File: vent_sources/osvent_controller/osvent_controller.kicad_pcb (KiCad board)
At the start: 2 copper layers, 151.1 x 76.8 mm, 56 parts, among them J1 SOLENOID_A, J2 SWITCH_A, J3 SWITCH_B, J4 SOLENOID_B, J5 POWER, J6 STEPPER, J7 PRESSURE_SENSOR, J8 TFT_DISPLAY, J9 SPEAKER, K1 G5V-2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

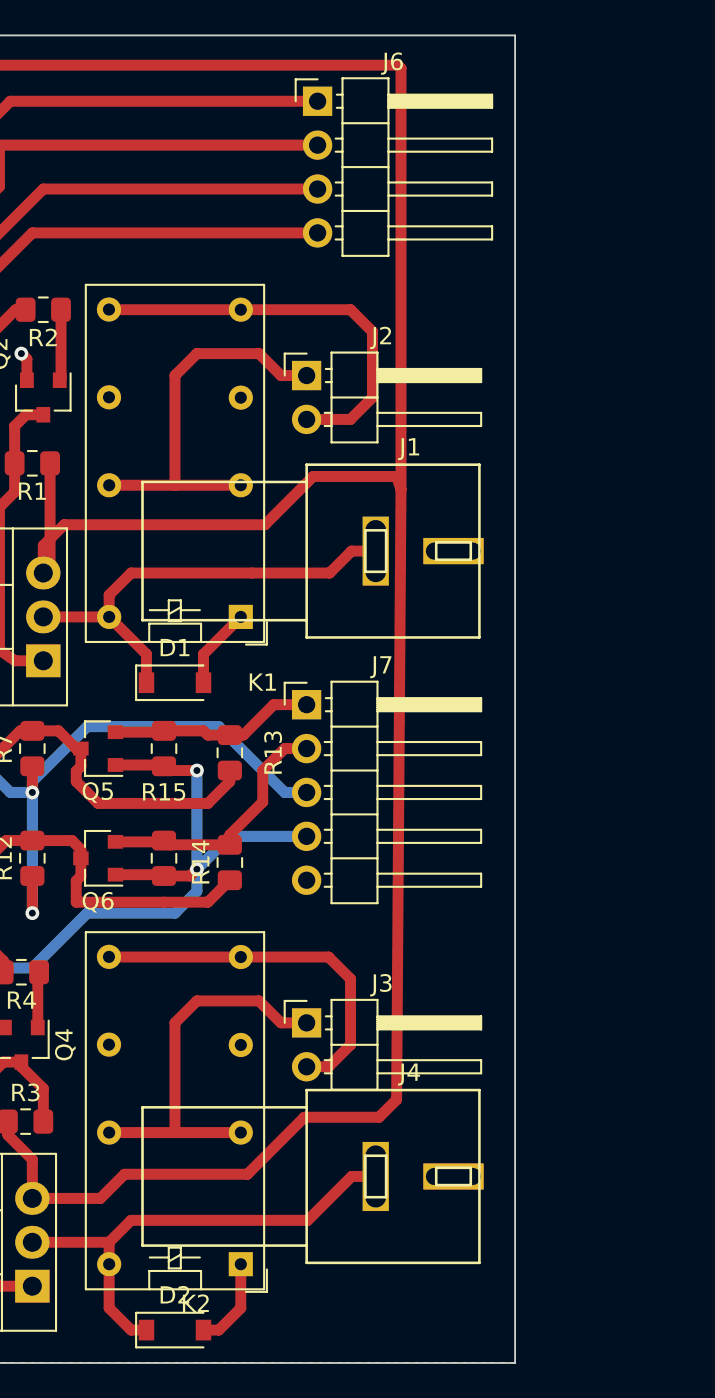
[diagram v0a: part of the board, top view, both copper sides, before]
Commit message: Flipped the RCA connectors around
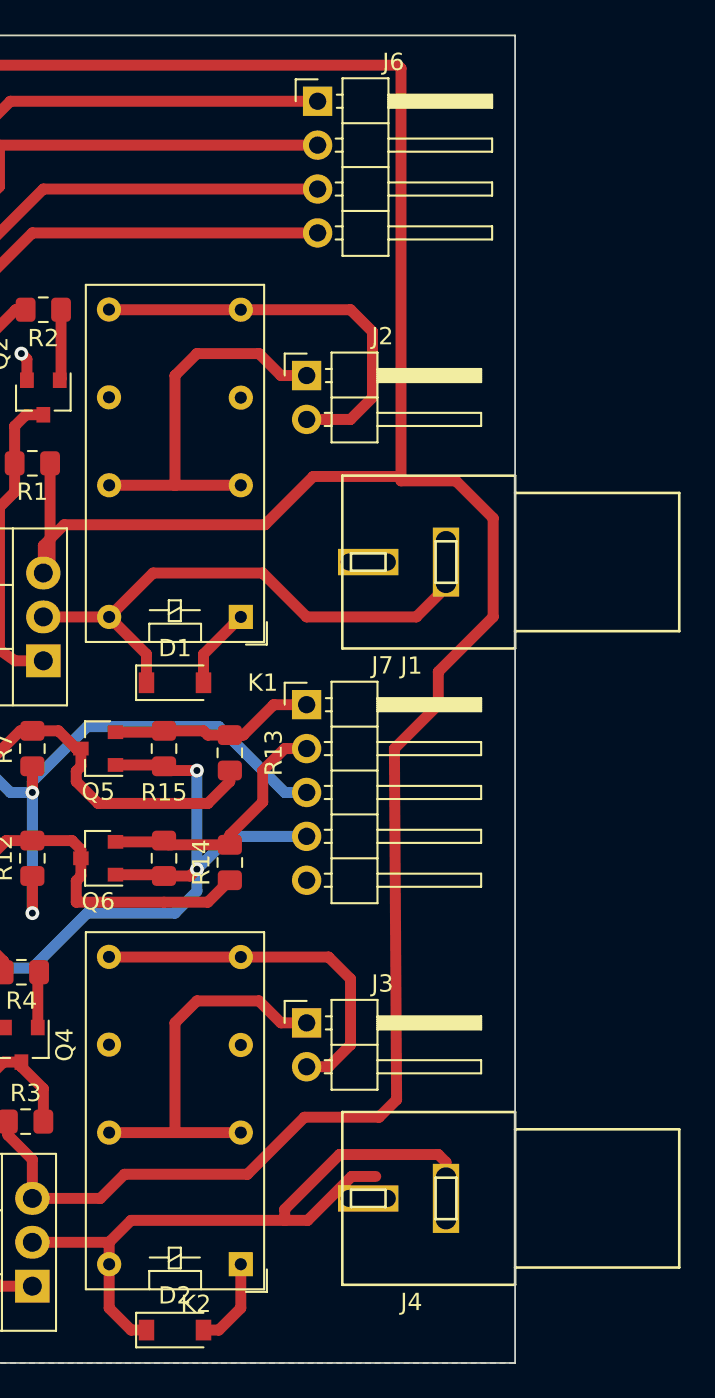
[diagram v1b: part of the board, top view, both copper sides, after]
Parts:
- moved J4 12.1 mm to (171.4, 89.5), turned to 180 degrees
- moved J1 12.1 mm to (171.4, 52.7), turned to 180 degrees
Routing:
- net Net-(D2-Pad1): track 27.9 -> 41.5 mm
- net Net-(D1-Pad1): track 26.3 -> 32.3 mm
- net +12V: track 247.0 -> 252.6 mm
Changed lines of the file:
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@@
     (thickness 1.6)
     (drawings 4)
-    (tracks 570)
+    (tracks 581)
     (zones 0)
     (modules 56)
@@
   )
   (module library:Kycon_KLPX-0848A-2-x (layer F.Cu)
-    (at 159.385 52.07)
+    (at 171.45 52.705 180)
     (fp_text reference J1 (at 6 -6 180) (layer F.SilkS)
       (effects (font (size 1 1) (thickness 0.15)))
@@
     (fp_line (start 0 -5) (end 10 -5) (layer F.SilkS) (width 0.15))
     (fp_line (start 0 -4) (end 0 -5) (layer F.SilkS) (width 0.15))
-    (pad 1 thru_hole rect (at 8.5 0) (size 3.5 1.524) (drill oval 3.2 1) (layers *.Cu *.Mask)
+    (pad 1 thru_hole rect (at 8.5 0 180) (size 3.5 1.524) (drill oval 3.2 1) (layers *.Cu *.Mask)
       (net 5 GNDREF))
-    (pad 2 thru_hole rect (at 4 0) (size 1.524 4) (drill oval 1.2 3.6) (layers *.Cu *.Mask)
+    (pad 2 thru_hole rect (at 4 0 180) (size 1.524 4) (drill oval 1.2 3.6) (layers *.Cu *.Mask)
       (net 45 "Net-(D1-Pad1)"))
   )
@@
   )
   (module library:Kycon_KLPX-0848A-2-x (layer F.Cu)
-    (at 159.385 88.265)
+    (at 171.45 89.535 180)
     (fp_text reference J4 (at 6 -6 180) (layer F.SilkS)
       (effects (font (size 1 1) (thickness 0.15)))
@@
     (fp_line (start 0 -5) (end 10 -5) (layer F.SilkS) (width 0.15))
     (fp_line (start 0 -4) (end 0 -5) (layer F.SilkS) (width 0.15))
-    (pad 1 thru_hole rect (at 8.5 0) (size 3.5 1.524) (drill oval 3.2 1) (layers *.Cu *.Mask)
+    (pad 1 thru_hole rect (at 8.5 0 180) (size 3.5 1.524) (drill oval 3.2 1) (layers *.Cu *.Mask)
       (net 5 GNDREF))
-    (pad 2 thru_hole rect (at 4 0) (size 1.524 4) (drill oval 1.2 3.6) (layers *.Cu *.Mask)
+    (pad 2 thru_hole rect (at 4 0 180) (size 1.524 4) (drill oval 1.2 3.6) (layers *.Cu *.Mask)
       (net 46 "Net-(D2-Pad1)"))
   )
@@
   (segment (start 142.095 85.09) (end 142.095 85.87) (width 0.635) (layer F.Cu) (net 30))
   (segment (start 142.095 85.87) (end 143.51 87.285) (width 0.635) (layer F.Cu) (net 30))
-  (segment (start 144.145 51.7525) (end 144.145 53.34) (width 0.635) (layer F.Cu) (net 30))
-  (segment (start 145.3515 50.546) (end 144.145 51.7525) (width 0.635) (layer F.Cu) (net 30))
-  (segment (start 156.972 50.546) (end 145.3515 50.546) (width 0.635) (layer F.Cu) (net 30))
-  (segment (start 159.766 47.752) (end 156.972 50.546) (width 0.635) (layer F.Cu) (net 30))
-  (segment (start 164.592 47.752) (end 159.766 47.752) (width 0.635) (layer F.Cu) (net 30))
   (segment (start 143.51 89.535) (end 147.447 89.535) (width 0.635) (layer F.Cu) (net 30))
   (segment (start 155.956 88.138) (end 159.258 84.836) (width 0.635) (layer F.Cu) (net 30))
@@
   (segment (start 139.88099 23.94901) (end 164.66501 23.94901) (width 0.635) (layer F.Cu) (net 30))
   (segment (start 137.16 26.67) (end 139.88099 23.94901) (width 0.635) (layer F.Cu) (net 30))
-  (segment (start 164.846 24.13) (end 164.846 48.514) (width 0.635) (layer F.Cu) (net 30))
-  (segment (start 164.592 83.82) (end 164.846 48.514) (width 0.635) (layer F.Cu) (net 30))
   (segment (start 164.66501 23.94901) (end 164.846 24.13) (width 0.635) (layer F.Cu) (net 30))
-  (segment (start 164.846 48.514) (end 164.592 47.752) (width 0.635) (layer F.Cu) (net 30))
   (segment (start 63.5 26.035) (end 63.5 33.02) (width 0.635) (layer F.Cu) (net 30))
   (segment (start 65.659 23.876) (end 63.5 26.035) (width 0.635) (layer F.Cu) (net 30))
   (segment (start 137.16 26.67) (end 134.366 23.876) (width 0.635) (layer F.Cu) (net 30))
   (segment (start 134.366 23.876) (end 65.659 23.876) (width 0.635) (layer F.Cu) (net 30))
+  (segment (start 164.846 48.006) (end 168.021 48.006) (width 0.635) (layer F.Cu) (net 30))
+  (segment (start 164.846 24.13) (end 164.846 48.006) (width 0.635) (layer F.Cu) (net 30))
+  (segment (start 168.021 48.006) (end 170.18 50.165) (width 0.635) (layer F.Cu) (net 30))
+  (segment (start 170.18 50.165) (end 170.18 55.88) (width 0.635) (layer F.Cu) (net 30))
+  (segment (start 170.18 55.88) (end 167.005 59.055) (width 0.635) (layer F.Cu) (net 30))
+  (segment (start 167.005 59.055) (end 167.005 60.96) (width 0.635) (layer F.Cu) (net 30))
+  (segment (start 167.005 60.96) (end 164.465 63.5) (width 0.635) (layer F.Cu) (net 30))
+  (segment (start 164.592 83.82) (end 164.465 63.5) (width 0.635) (layer F.Cu) (net 30))
+  (segment (start 164.592 47.752) (end 159.766 47.752) (width 0.635) (layer F.Cu) (net 30))
+  (segment (start 159.766 47.752) (end 156.972 50.546) (width 0.635) (layer F.Cu) (net 30))
+  (segment (start 156.972 50.546) (end 145.3515 50.546) (width 0.635) (layer F.Cu) (net 30))
+  (segment (start 145.3515 50.546) (end 144.145 51.7525) (width 0.635) (layer F.Cu) (net 30))
+  (segment (start 144.145 51.7525) (end 144.145 53.34) (width 0.635) (layer F.Cu) (net 30))
   (segment (start 160.02 26.035) (end 142.24 26.035) (width 0.635) (layer F.Cu) (net 31))
   (segment (start 142.24 26.035) (end 140.335 27.94) (width 0.635) (layer F.Cu) (net 31))
@@
   (segment (start 88.225 29.25) (end 97.79 29.25) (width 0.635) (layer F.Cu) (net 44))
   (segment (start 85.725 31.75) (end 88.225 29.25) (width 0.635) (layer F.Cu) (net 44))
-  (segment (start 149.225 53.34) (end 147.955 54.61) (width 0.635) (layer F.Cu) (net 45))
   (segment (start 150.115 59.69) (end 150.115 58.04) (width 0.635) (layer F.Cu) (net 45))
-  (segment (start 147.955 54.61) (end 147.955 55.88) (width 0.635) (layer F.Cu) (net 45))
   (segment (start 150.115 58.04) (end 147.955 55.88) (width 0.635) (layer F.Cu) (net 45))
   (segment (start 147.955 55.88) (end 144.145 55.88) (width 0.635) (layer F.Cu) (net 45))
-  (segment (start 161.988 52.07) (end 160.718 53.34) (width 0.635) (layer F.Cu) (net 45))
-  (segment (start 160.718 53.34) (end 156.21 53.34) (width 0.635) (layer F.Cu) (net 45))
-  (segment (start 163.385 52.07) (end 161.988 52.07) (width 0.635) (layer F.Cu) (net 45))
-  (segment (start 156.21 53.34) (end 149.225 53.34) (width 0.635) (layer F.Cu) (net 45))
+  (segment (start 167.45 52.705) (end 167.45 54.165) (width 0.635) (layer F.Cu) (net 45))
+  (segment (start 167.45 54.165) (end 165.735 55.88) (width 0.635) (layer F.Cu) (net 45))
+  (segment (start 165.735 55.88) (end 159.385 55.88) (width 0.635) (layer F.Cu) (net 45))
+  (segment (start 159.385 55.88) (end 156.845 53.34) (width 0.635) (layer F.Cu) (net 45))
+  (segment (start 156.845 53.34) (end 150.495 53.34) (width 0.635) (layer F.Cu) (net 45))
+  (segment (start 150.495 53.34) (end 147.955 55.88) (width 0.635) (layer F.Cu) (net 45))
   (segment (start 147.955 95.885) (end 149.225 97.155) (width 0.635) (layer F.Cu) (net 46))
   (segment (start 147.955 92.075) (end 147.955 93.345) (width 0.635) (layer F.Cu) (net 46))
@@
   (segment (start 147.955 93.345) (end 147.955 95.885) (width 0.635) (layer F.Cu) (net 46))
   (segment (start 149.225 90.805) (end 147.955 92.075) (width 0.635) (layer F.Cu) (net 46))
-  (segment (start 159.448 90.805) (end 149.225 90.805) (width 0.635) (layer F.Cu) (net 46))
   (segment (start 161.988 88.265) (end 159.448 90.805) (width 0.635) (layer F.Cu) (net 46))
   (segment (start 163.385 88.265) (end 161.988 88.265) (width 0.635) (layer F.Cu) (net 46))
+  (segment (start 158.115 90.805) (end 149.225 90.805) (width 0.635) (layer F.Cu) (net 46))
+  (segment (start 159.448 90.805) (end 158.115 90.805) (width 0.635) (layer F.Cu) (net 46))
+  (segment (start 167.45 87.44) (end 167.45 89.535) (width 0.635) (layer F.Cu) (net 46))
+  (segment (start 167.005 86.995) (end 167.45 87.44) (width 0.635) (layer F.Cu) (net 46))
+  (segment (start 161.29 86.995) (end 167.005 86.995) (width 0.635) (layer F.Cu) (net 46))
+  (segment (start 158.115 90.805) (end 158.115 90.17) (width 0.635) (layer F.Cu) (net 46))
+  (segment (start 158.115 90.17) (end 161.29 86.995) (width 0.635) (layer F.Cu) (net 46))
   (segment (start 159.385 44.45) (end 161.925 44.45) (width 0.635) (layer F.Cu) (net 47))
   (segment (start 161.925 38.1) (end 155.575 38.1) (width 0.635) (layer F.Cu) (net 47))
@@
     (connect_pads (clearance 0.508))
     (min_thickness 0.254)
-    (fill yes (arc_segments 32) (thermal_gap 0.508) (thermal_bridge_width 0.508))
+    (fill (arc_segments 32) (thermal_gap 0.508) (thermal_bridge_width 0.508))
     (polygon
       (pts

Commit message: Removed relays, added extra connector, surge cap
1. Removed the PCB mounted relays. Instead use outboard relays of appropriate rating.
2. Added a 47uf close to A4988 to protect from ESD/surge
3. Added a new connector with A6,A7, D7, +5 and ground for analog sensors
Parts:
- removed J2: SWITCH_A, Connector_PinHeader_2.54mm:PinHeader_1x02_P2.54mm_Horizontal
- removed J3: SWITCH_B, Connector_PinHeader_2.54mm:PinHeader_1x02_P2.54mm_Horizontal
- removed K1, K2: G5V-2, Relay_THT:Relay_DPDT_Omron_G5V-2
- added C10: 47u, Capacitor_THT:CP_Radial_D5.0mm_P2.50mm, F.Cu at (143.5, 28.6)
- added J10: EXTENSION PORT, Connector_PinHeader_2.54mm:PinHeader_1x05_P2.54mm_Horizontal, F.Cu at (159.4, 76.2)
- moved J6 7.62 mm to (160.0, 33.7)
- moved D2 7.24 mm to (156.2, 91.4), turned to 180 degrees
- moved J4 4.62 mm to (170.2, 94.0)
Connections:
- A1 pad 10: Net-(A1-Pad10) -> EXTRA
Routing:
- net Net-(A1-Pad26): track 0.00 -> 74.2 mm, vias 0 -> 3
- net EXTRA: track 0.00 -> 64.0 mm, vias 0 -> 3
- net Net-(A1-Pad25): track 0.00 -> 63.8 mm, vias 0 -> 1
- net Net-(J2-Pad2): track 23.9 -> 0.00 mm
- net Net-(J2-Pad1): track 22.6 -> 0.00 mm
- net Net-(J3-Pad1): track 22.6 -> 0.00 mm
- net Net-(J3-Pad2): track 21.4 -> 0.00 mm
- net +5V: track 322.9 -> 339.7 mm, vias 6 -> 8
- net Net-(D2-Pad1): track 41.5 -> 27.5 mm, vias 0 -> 2
- net GNDREF: track 127.4 -> 121.0 mm, vias 5 -> 7
- net +12V: track 252.6 -> 257.8 mm
- net Net-(A2-Pad6): track 26.7 -> 24.2 mm
- net Net-(A2-Pad3): track 25.5 -> 27.7 mm
- net Net-(A2-Pad4): track 25.2 -> 26.7 mm
- net Net-(A2-Pad5): track 26.6 -> 25.2 mm
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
